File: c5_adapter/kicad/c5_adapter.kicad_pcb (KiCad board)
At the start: 2 copper layers, 2 parts, among them IC1 TLV6700DDCR, J2 Conn_01x10

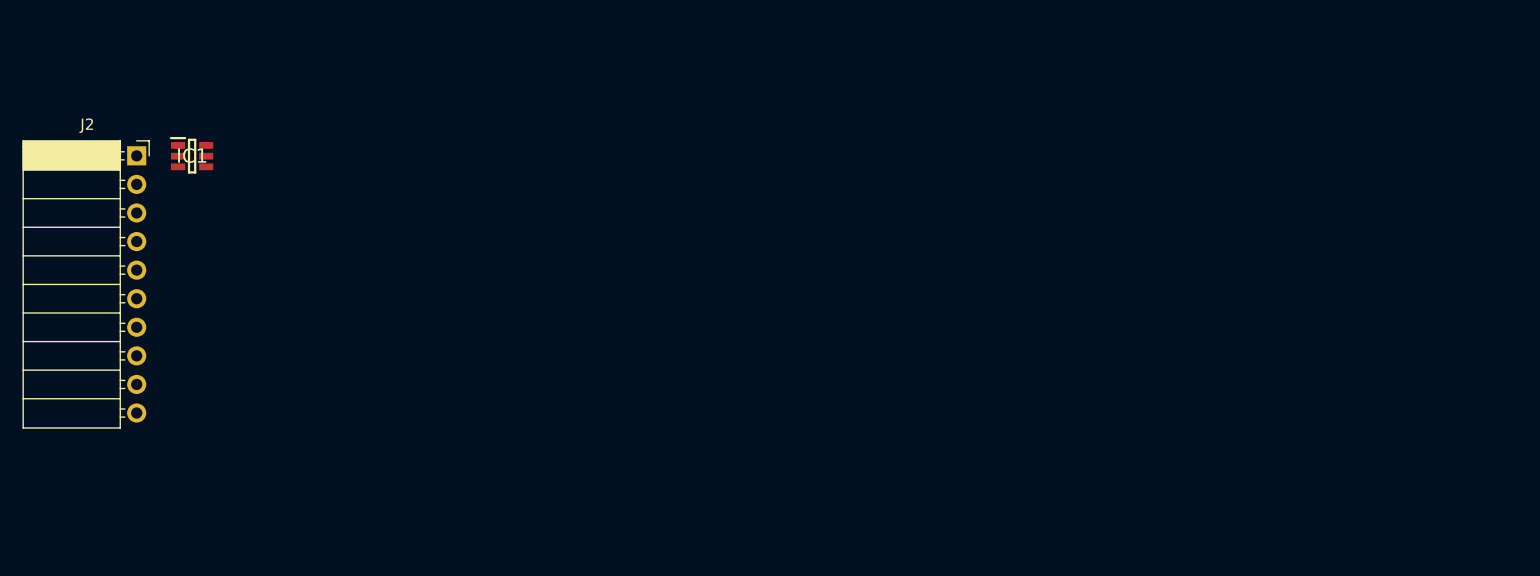
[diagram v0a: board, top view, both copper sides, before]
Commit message: Initial PCB placement
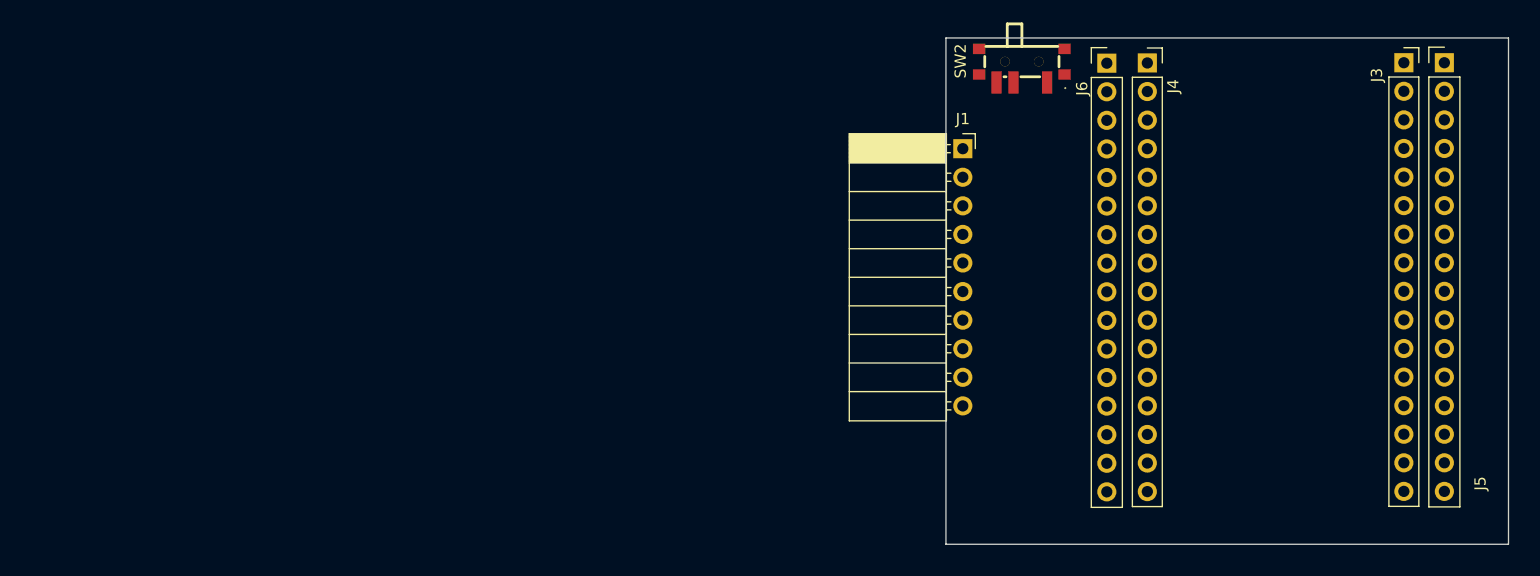
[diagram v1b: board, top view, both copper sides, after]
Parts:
- removed IC1: TLV6700DDCR, TLV6700DDCR:SOT95P280X110-6N
- removed J2: Conn_01x10, Connector_PinSocket_2.54mm:PinSocket_1x10_P2.54mm_Horizontal
- added J1: Conn_01x10, Connector_PinSocket_2.54mm:PinSocket_1x10_P2.54mm_Horizontal, F.Cu at (174.5, 88.7)
- added J3: Conn_01x16, Connector_PinSocket_2.54mm:PinSocket_1x16_P2.54mm_Vertical, F.Cu at (213.7, 81.1)
- added J4: Conn_01x16, Connector_PinSocket_2.54mm:PinSocket_1x16_P2.54mm_Vertical, F.Cu at (190.9, 81.1)
- added J5: Conn_01x16, Connector_PinHeader_2.54mm:PinHeader_1x16_P2.54mm_Vertical, F.Cu at (217.3, 81.1)
- added J6: Conn_01x16, Connector_PinHeader_2.54mm:PinHeader_1x16_P2.54mm_Vertical, F.Cu at (187.3, 81.1)
- added SW2: MK-12C02-G020, C5-Addon:SW-SMD_MK-12C02-G020, F.Cu at (179.8, 81.4)
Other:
- board outline added: 50 x 45 mm

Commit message: Updated c5 adapter PCB placement
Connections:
- J4 pad 10: Net-(J4-Pin_10) -> IO6
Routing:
- net IO10: track 0.00 -> 52.9 mm, vias 0 -> 1
- net BOOT: track 0.00 -> 49.0 mm
- net IO9: track 0.00 -> 48.9 mm, vias 0 -> 1
- net UART_TX: track 0.00 -> 48.1 mm
- net UART_RX: track 0.00 -> 48.1 mm
- net IO8: track 0.00 -> 44.9 mm
- net RST: track 0.00 -> 22.5 mm
- net +3V3: track 0.00 -> 20.2 mm
- net IO6: track 0.00 -> 17.5 mm
- net VIO_{DOCK}: track 0.00 -> 12.7 mm
- net GND: track 0.00 -> 10.8 mm, vias 0 -> 15
- net Net-(J4-Pin_6): track 0.00 -> 3.61 mm
- net Net-(J4-Pin_13): track 0.00 -> 3.61 mm
- net Net-(J4-Pin_11): track 0.00 -> 3.61 mm
- net Net-(J4-Pin_4): track 0.00 -> 3.61 mm
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- added copper zone on B.Cu, net GND
- added copper zone on F.Cu, net GND
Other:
- copper layers 2 -> 4
- board text added: "C5 Devkit Adapter"

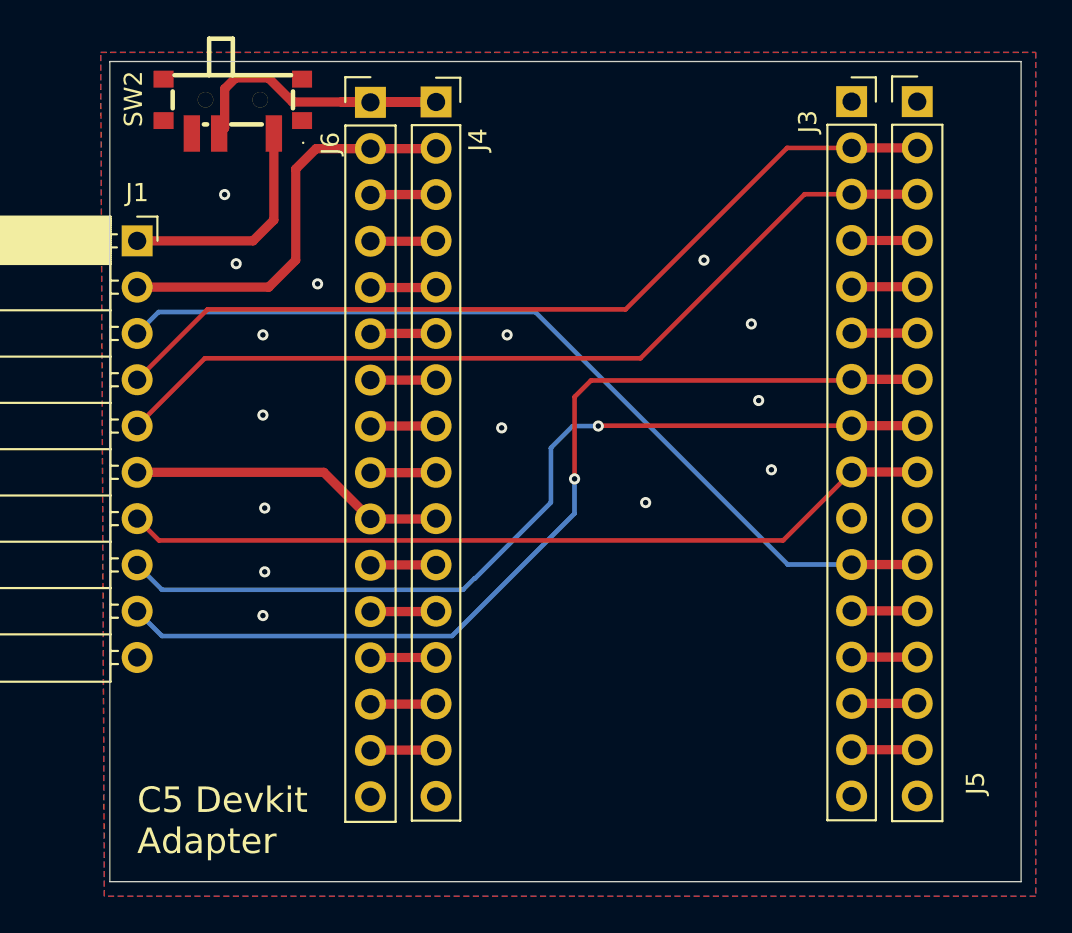
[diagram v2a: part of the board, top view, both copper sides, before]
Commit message: Updated silkscreen on C5 adapter
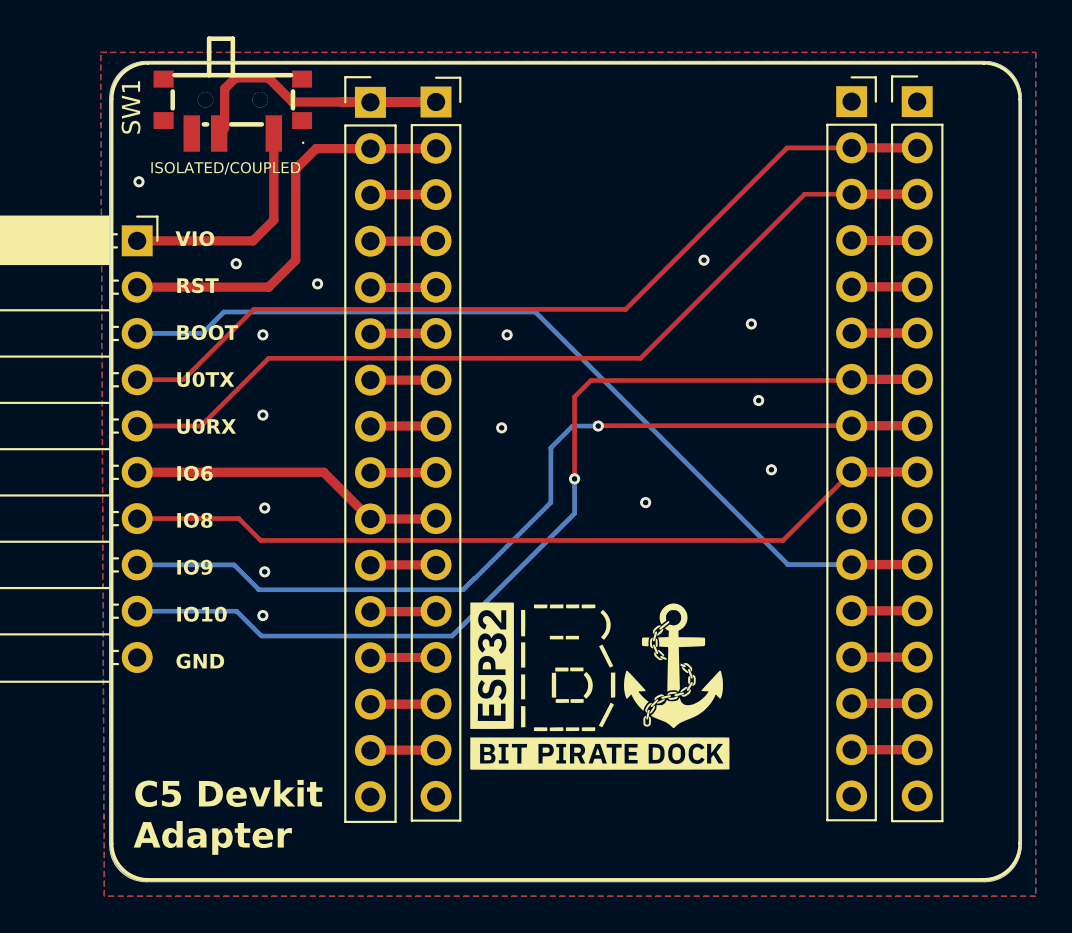
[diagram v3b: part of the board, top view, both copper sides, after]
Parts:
- added G***: LOGO, LOGO, F.Cu at (200.0, 112.8)
- renumbered J6 to J3, J3 to J5, J5 to J6, SW2 to SW1
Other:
- outline, holes or cut-outs redrawn
- board text added: "ISOLATED/COUPLED"
- board text added: "VIO RST BOOT U0TX U0RX IO6 IO8 IO9 IO10 GND"
